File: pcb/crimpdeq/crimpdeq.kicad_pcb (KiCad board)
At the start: 4 copper layers, 30 x 30 mm, 55 parts, among them J10 A-_Cable_Pad, J11 E+_Cable_Pad, J12 E-_Cable_Pad, J2 USB4105-GF-A, J5 B-_Cable_Pad, J6 SW+_Cable_Pad, J7 B+_Cable_Pad, J8 SW-_Cable_Pad, J9 A+_Cable_Pad, Q2 DMG3415U, U1 ESP32-C3-MINI-1, U2 MCP73831T-2ACI/OT, U3 ADS1220, U5 MAX17048G+T10, U6 SY8088

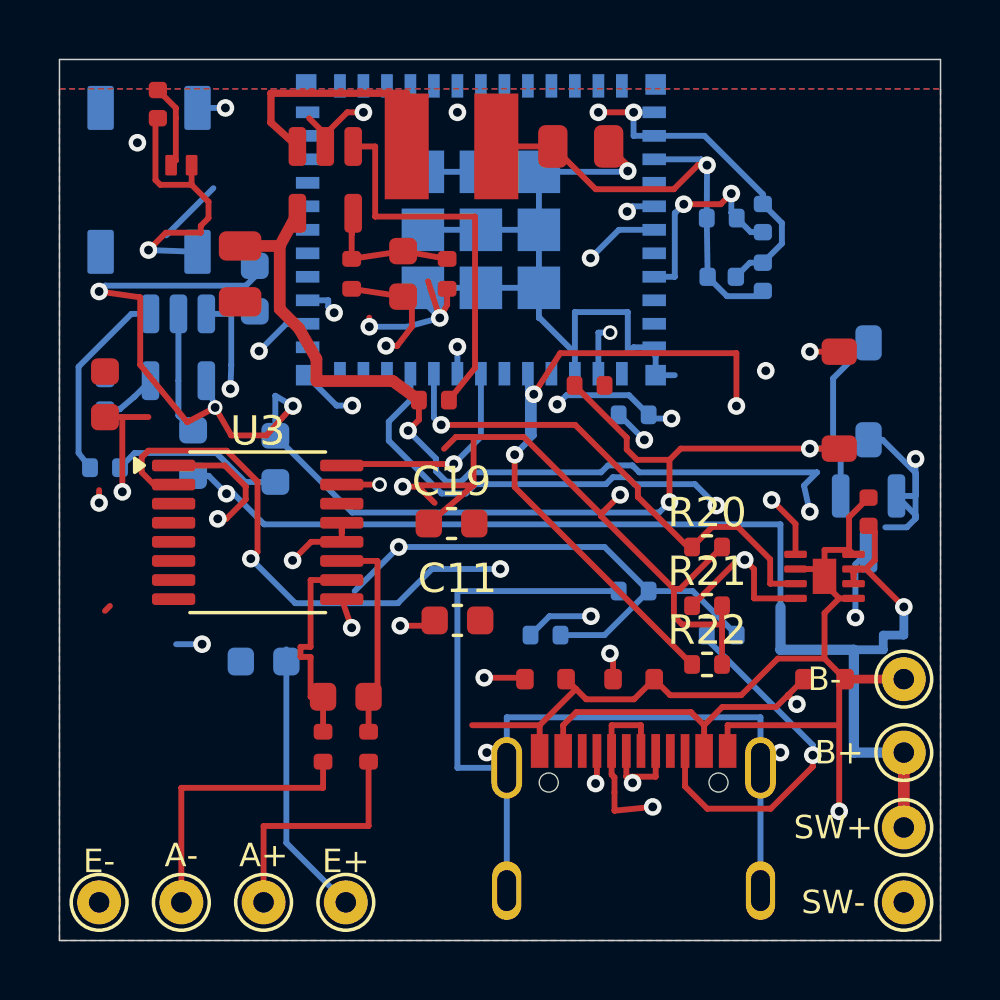
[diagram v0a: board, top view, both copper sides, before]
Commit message: fix: improve ADC bypassing and reconcile assembly metadata
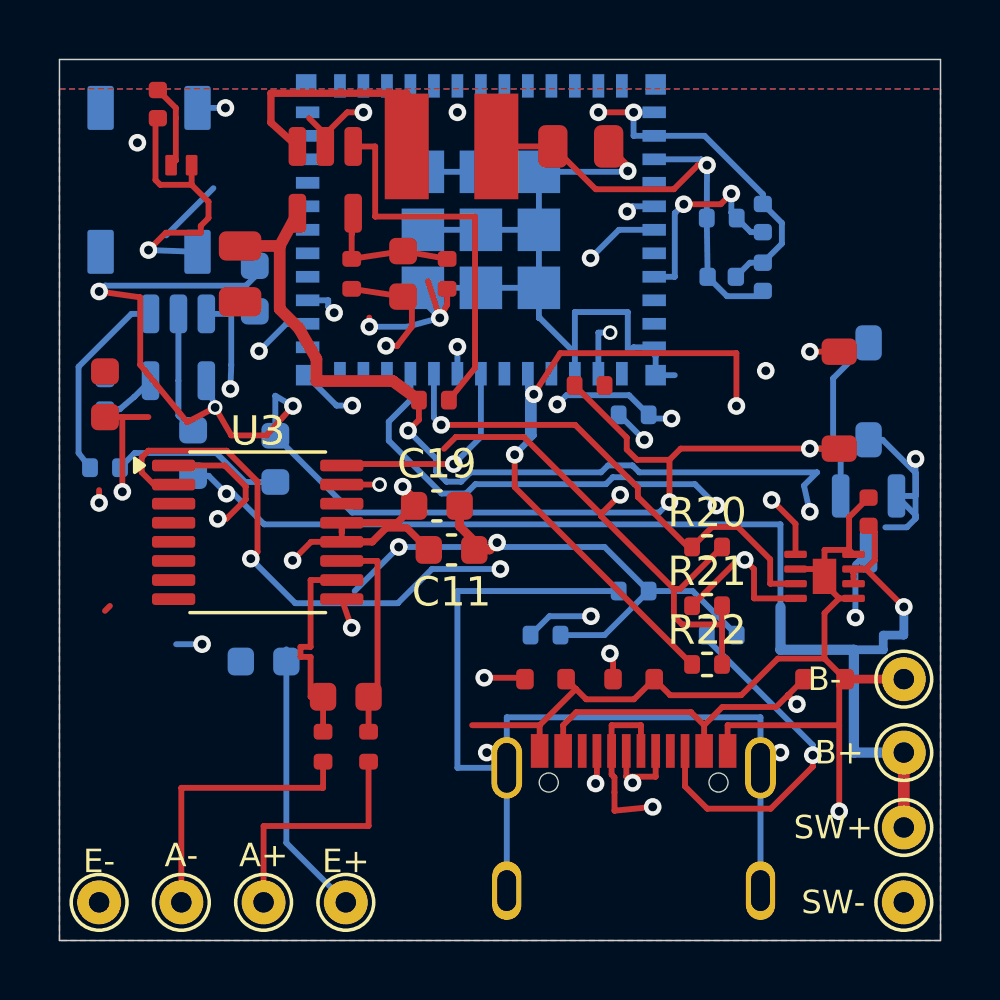
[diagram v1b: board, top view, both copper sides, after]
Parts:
- moved C11 2.41 mm to (140.8, 69.1)
- moved C19 0.78 mm to (140.3, 67.6)
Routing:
- net GND: track 134.6 -> 137.2 mm, vias 12 -> 13
- net IO5_SCK: track 26.4 -> 24.4 mm
- net +3V3: track 126.6 -> 124.8 mm, vias 10 -> 9
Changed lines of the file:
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@@
 			)
 		)
-		(property "LCSC" "C25741"
+		(property "LCSC" "C25076"
 			(at 0 0 270)
 			(unlocked yes)
@@
 	(footprint "C_0603_1608Metric"
 		(layer "F.Cu")
-		(at 141 71.5)
+		(at 140.8 69.1)
 		(descr "Capacitor SMD 0603 (1608 Metric), square (rectangular) end terminal, IPC-7351 nominal, (Body size source: IPC-SM-782 page 76, https://www.pcb-3d.com/wordpress/wp-content/uploads/ipc-sm-782a_amendment_1_and_2.pdf)")
 		(tags "capacitor")
 		(property "Reference" "C11"
-			(at 0 -1.43 0)
+			(at 0 1.43 0)
 			(layer "F.SilkS")
 			(effects
@@
 			)
 		)
-		(property "LCSC" "C25741"
+		(property "LCSC" "C25076"
 			(at 0 0 90)
 			(unlocked yes)
@@
 	(footprint "C_0603_1608Metric"
 		(layer "F.Cu")
-		(at 140.8 68.2)
+		(at 140.3 67.6)
 		(descr "Capacitor SMD 0603 (1608 Metric), square (rectangular) end terminal, IPC-7351 nominal, (Body size source: IPC-SM-782 page 76, https://www.pcb-3d.com/wordpress/wp-content/uploads/ipc-sm-782a_amendment_1_and_2.pdf)")
 		(tags "capacitor")
@@
 	)
 	(segment
+		(start 141.575 68.8)
+		(end 141.575 69.1)
+		(width 0.3)
+		(layer "F.Cu")
+		(net "GND")
+	)
+	(segment
 		(start 137.8 54.2)
 		(end 137.249 54.2)
@@
 	)
 	(segment
+		(start 141.075 68.3)
+		(end 141.575 68.8)
+		(width 0.3)
+		(layer "F.Cu")
+		(net "GND")
+	)
+	(segment
 		(start 154 73.7)
 		(end 154.2 73.5)
@@
 	)
 	(segment
+		(start 141.575 69.1)
+		(end 142.1 69.1)
+		(width 0.3)
+		(layer "F.Cu")
+		(net "GND")
+	)
+	(segment
 		(start 154.336 69.0983)
 		(end 154.488 69.25)
@@
 	)
 	(segment
+		(start 142.1 69.1)
+		(end 142.35 68.85)
+		(width 0.3)
+		(layer "F.Cu")
+		(net "GND")
+	)
+	(segment
+		(start 141.075 67.6)
+		(end 141.075 68.3)
+		(width 0.3)
+		(layer "F.Cu")
+		(net "GND")
+	)
+	(segment
 		(start 154 78)
 		(end 154 75.0683)
@@
 		(net "GND")
 	)
+	(via
+		(at 142.35 68.85)
+		(size 0.6)
+		(drill 0.3)
+		(layers "F.Cu" "B.Cu")
+		(net "GND")
+	)
 	(segment
 		(start 145 63.1)
@@
 	)
 	(segment
-		(start 141.55 65.256)
-		(end 141.55 66.9)
-		(width 0.2)
-		(layer "F.Cu")
-		(net "+3V3")
-	)
-	(segment
-		(start 141.55 66.9)
-		(end 139.671 66.9)
-		(width 0.2)
-		(layer "F.Cu")
-		(net "+3V3")
-	)
-	(segment
-		(start 140.025 68.2)
-		(end 141.55 66.9)
-		(width 0.2)
+		(start 139.525 67.3338)
+		(end 139.525 67.6)
+		(width 0.25)
 		(layer "F.Cu")
 		(net "+3V3")
 	)
 	(segment
-		(start 140.044 71.6807)
-		(end 139.054 71.6807)
-		(width 0.2)
+		(start 137.0625 68.825)
+		(end 138.1 68.825)
+		(width 0.25)
 		(layer "F.Cu")
 		(net "+3V3")
@@
 	)
 	(segment
-		(start 140.946 65.256)
-		(end 141.55 65.256)
+		(start 130.881 56.6686)
+		(end 131.95 56.6686)
 		(width 0.2)
 		(layer "F.Cu")
@@
 	)
 	(segment
-		(start 140.225 67.5)
-		(end 139.671 66.9458)
-		(width 0.2)
+		(start 138.575 68.35)
+		(end 139.275 68.35)
+		(width 0.25)
 		(layer "F.Cu")
 		(net "+3V3")
 	)
 	(segment
-		(start 130.881 56.6686)
-		(end 131.95 56.6686)
-		(width 0.2)
+		(start 138.1 68.825)
+		(end 138.575 68.35)
+		(width 0.25)
 		(layer "F.Cu")
 		(net "+3V3")
@@
 	)
 	(segment
-		(start 139.054 71.6807)
-		(end 139.054 71.6819)
-		(width 0.2)
+		(start 139.275 68.35)
+		(end 140.025 69.1)
+		(width 0.25)
 		(layer "F.Cu")
 		(net "+3V3")
@@
 	)
 	(segment
-		(start 139.671 66.9458)
-		(end 139.137 66.9458)
-		(width 0.2)
-		(layer "F.Cu")
-		(net "+3V3")
-	)
-	(segment
 		(start 150.01 71)
 		(end 150.01 71.6379)
@@
 	)
 	(segment
-		(start 139.671 66.9)
-		(end 139.671 66.9458)
-		(width 0.2)
-		(layer "F.Cu")
-		(net "+3V3")
-	)
-	(segment
 		(start 137.4 60.21)
 		(end 139.15 60.475)
@@
 	)
 	(segment
-		(start 129.591 67.1225)
-		(end 129.591 64.575)
-		(width 0.2)
+		(start 138.95 68.175)
+		(end 139.525 67.6)
+		(width 0.25)
 		(layer "F.Cu")
 		(net "+3V3")
 	)
 	(segment
-		(start 149.186 56)
-		(end 148.367 56.8187)
+		(start 129.591 67.1225)
+		(end 129.591 64.575)
 		(width 0.2)
 		(layer "F.Cu")
@@
 	)
 	(segment
-		(start 140.225 71.5)
-		(end 140.044 71.6807)
+		(start 149.186 56)
+		(end 148.367 56.8187)
 		(width 0.2)
 		(layer "F.Cu")
@@
 	)
 	(segment
-		(start 139.671 66.9458)
-		(end 139.671 66.946)
-		(width 0.2)
+		(start 139.137 66.9458)
+		(end 139.525 67.3338)
+		(width 0.25)
 		(layer "F.Cu")
 		(net "+3V3")
@@
 	)
 	(segment
+		(start 137.0625 68.175)
+		(end 138.95 68.175)
+		(width 0.25)
+		(layer "F.Cu")
+		(net "+3V3")
+	)
+	(segment
 		(start 136.02 68.825)
 		(end 136.541 68.825)
@@
 	)
 	(via
-		(at 139.054 71.6819)
-		(size 0.6)
-		(drill 0.3)
-		(layers "F.Cu" "B.Cu")
-		(net "+3V3")
-	)
-	(via
 		(at 137.4 71.75)
 		(size 0.6)
@@
 		(width 0.2)
 		(layer "In2.Cu")
-		(net "IO5_SCK")
-	)
-	(segment
-		(start 139.66 63.5214)
-		(end 138.216 64.9659)
-		(width 0.2)
-		(layer "In2.Cu")

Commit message: fix: keep digital routing outside ADC inputs
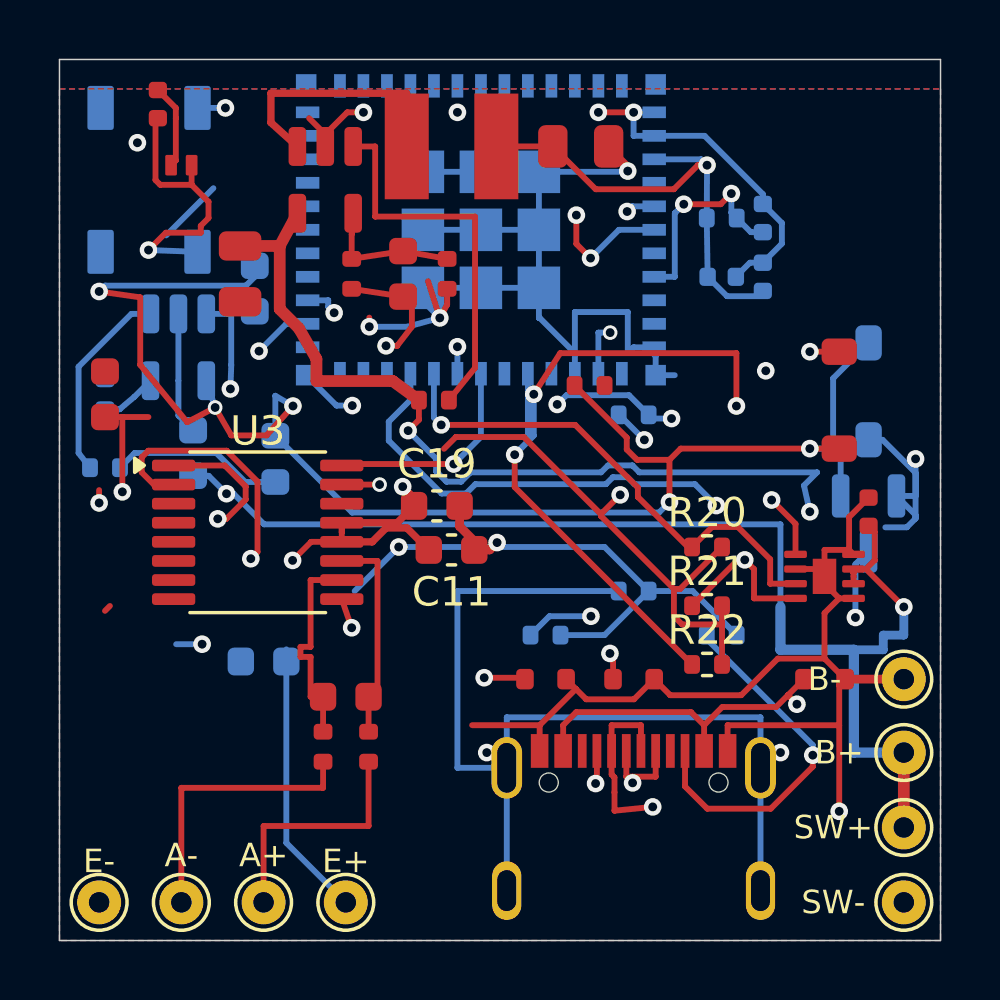
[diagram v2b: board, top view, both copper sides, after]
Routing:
- net IO3_CS: track 33.0 -> 37.6 mm
- net USB_D-: track 41.5 -> 40.2 mm
- net USB_D+: track 41.5 -> 40.9 mm
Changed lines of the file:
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@@
-	)
-	(segment
-		(start 136.802 70.4)
-		(end 136.802 61.026)
-		(width 0.2)
-		(layer "In2.Cu")
-		(net "USB_D+")
 	)
 	(segment
@@
 	)
 	(segment
-		(start 146.194 70.4)
-		(end 136.802 70.4)
+		(start 136.802 61.026)
+		(end 136.802 67.45)
+		(width 0.2)
+		(layer "In2.Cu")
+		(net "USB_D+")
+	)
+	(segment
+		(start 146.194 68.45)
+		(end 146.194 72.6247)
 		(width 0.2)
 		(layer "In2.Cu")
@@
 	)
 	(segment
+		(start 145.694 67.95)
+		(end 146.194 68.45)
+		(width 0.2)
+		(layer "In2.Cu")
+		(net "USB_D+")
+	)
+	(segment
 		(start 148.55 74.2)
 		(end 148.55 73.4)
@@
 	)
 	(segment
+		(start 137.302 67.95)
+		(end 145.694 67.95)
+		(width 0.2)
+		(layer "In2.Cu")
+		(net "USB_D+")
+	)
+	(segment
 		(start 146.965 77.0322)
 		(end 146.965 75)
@@
 	)
 	(segment
+		(start 136.802 67.45)
+		(end 137.302 67.95)
+		(width 0.2)
+		(layer "In2.Cu")
+		(net "USB_D+")
+	)
+	(segment
 		(start 150.5 75)
 		(end 150.5 74.2)
@@
 		(start 146.965 72.6247)
 		(end 146.194 72.6247)
-		(width 0.2)
-		(layer "In2.Cu")
-		(net "USB_D+")
-	)
-	(segment
-		(start 146.194 72.6247)
-		(end 146.194 70.4)
 		(width 0.2)
 		(layer "In2.Cu")
@@
 	)
 	(segment
-		(start 134.245 68)
-		(end 134.245 62.331)
+		(start 141.95 69.55)
+		(end 144.4 69.55)
 		(width 0.2)
 		(layer "In2.Cu")
@@
 	)
 	(segment
+		(start 134.245 62.331)
+		(end 134.245 67.85)
+		(width 0.2)
+		(layer "In2.Cu")
+		(net "USB_D-")
+	)
+	(segment
+		(start 134.245 67.85)
+		(end 134.745 68.35)
+		(width 0.2)
+		(layer "In2.Cu")
+		(net "USB_D-")
+	)
+	(segment
+		(start 134.745 68.35)
+		(end 140.75 68.35)
+		(width 0.2)
+		(layer "In2.Cu")
+		(net "USB_D-")
+	)
+	(segment
 		(start 144.9 77.85)
-		(end 144.9 70.85)
+		(end 144.9 73.4517)
 		(width 0.2)
 		(layer "In2.Cu")
@@
 	)
 	(segment
-		(start 136.1 68)
-		(end 134.245 68)
+		(start 140.75 68.35)
+		(end 141.95 69.55)
 		(width 0.2)
 		(layer "In2.Cu")
@@
 	)
 	(segment
+		(start 144.9 70.05)
+		(end 144.9 73.4517)
+		(width 0.2)
+		(layer "In2.Cu")
+		(net "USB_D-")
+	)
+	(segment
 		(start 144.9 73.4517)
 		(end 141.912 73.4517)
@@
 	)
 	(segment
-		(start 136.1 70.85)
-		(end 136.1 68)
-		(width 0.2)
-		(layer "In2.Cu")
-		(net "USB_D-")
-	)
-	(segment
-		(start 144.9 70.85)
-		(end 136.1 70.85)
+		(start 144.4 69.55)
+		(end 144.9 70.05)
 		(width 0.2)
 		(layer "In2.Cu")
@@
 	)
 	(segment
+		(start 145.05 58.6793)
+		(end 145.05 57.7)
+		(width 0.2)
+		(layer "F.Cu")
+		(net "IO3_CS")
+	)
+	(segment
 		(start 130.25 65.949)
 		(end 130.25 66.4586)
@@
 	)
 	(segment
+		(start 145.534 59.1633)
+		(end 145.05 58.6793)
+		(width 0.2)
+		(layer "F.Cu")
+		(net "IO3_CS")
+	)
+	(segment
 		(start 134.193 69.1705)
 		(end 134.193 66.772)
@@
 	)
 	(via
-		(at 142.462 69.75)
-		(size 0.6)
-		(drill 0.3)
-		(layers "F.Cu" "B.Cu")
-		(net "IO3_CS")
-	)
-	(segment
-		(start 135.48 70.9141)
-		(end 133.965 69.3987)
-		(width 0.2)
-		(layer "B.Cu")
+		(at 145.05 57.7)
+		(size 0.6)
+		(drill 0.3)
+		(layers "F.Cu" "B.Cu")
 		(net "IO3_CS")
 	)
@@
 	)
 	(segment
-		(start 138.971 70.9141)
-		(end 135.48 70.9141)
-		(width 0.2)
-		(layer "B.Cu")
-		(net "IO3_CS")
-	)
-	(segment
 		(start 147.7 58.2)
 		(end 146.498 58.2)
@@
 	)
 	(segment
-		(start 142.462 69.75)
-		(end 140.135 69.75)
-		(width 0.2)
-		(layer "B.Cu")
+		(start 144.85 57.9)
+		(end 141.55 57.9)
+		(width 0.2)
+		(layer "In2.Cu")
 		(net "IO3_CS")
 	)
 	(segment
-		(start 140.135 69.75)
-		(end 138.971 70.9141)
-		(width 0.2)
-		(layer "B.Cu")
+		(start 132.1 68.65)
+		(end 132.8487 69.3987)
+		(width 0.2)
+		(layer "In2.Cu")
 		(net "IO3_CS")
 	)
 	(segment
-		(start 145.534 66.678)
-		(end 142.462 69.75)
+		(start 141.55 57.9)
+		(end 139.9 59.55)
 		(width 0.2)
 		(layer "In2.Cu")
@@
 	)
 	(segment
-		(start 145.534 59.1633)
-		(end 145.534 66.678)
-		(width 0.2)
-		(layer "In2.Cu")
+		(start 145.05 57.7)
+		(end 144.85 57.9)
+		(width 0.2)
+		(layer "In2.Cu")
+		(net "IO3_CS")
+	)
+	(segment
+		(start 131.1 67)
+		(end 132.1 68)
+		(width 0.2)
+		(layer "In2.Cu")
+		(net "IO3_CS")
+	)
+	(segment
+		(start 131.1 62.9)
+		(end 131.1 67)
+		(width 0.2)
+		(layer "In2.Cu")
+		(net "IO3_CS")
+	)
+	(segment
+		(start 132.1 68)
+		(end 132.1 68.65)
+		(width 0.2)
+		(layer "In2.Cu")
+		(net "IO3_CS")
+	)
+	(segment
+		(start 134.45 59.55)
+		(end 131.1 62.9)
+		(width 0.2)
+		(layer "In2.Cu")
+		(net "IO3_CS")
+	)
+	(segment
+		(start 139.9 59.55)
+		(end 134.45 59.55)
+		(width 0.2)
+		(layer "In2.Cu")
+		(net "IO3_CS")
+	)
+	(segment
+		(start 132.8487 69.3987)
+		(end 133.965 69.3987)
+		(width 0.2)
+		(layer "In2.Cu")

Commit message: fix: remove USB pair routing overlap
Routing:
- net USB_D+: track 40.9 -> 37.7 mm
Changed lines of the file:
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@@
 	)
 	(segment
-		(start 148.55 73.4)
-		(end 146.965 73.4)
-		(width 0.2)
-		(layer "In2.Cu")
-		(net "USB_D+")
-	)
-	(segment
-		(start 146.965 73.4)
-		(end 148.548 73.4)
+		(start 148.548 72.8)
+		(end 148.548 74.2)
 		(width 0.2)
 		(layer "In2.Cu")
@@
 	)
 	(segment
-		(start 148.548 73.4)
-		(end 148.548 72.8)
-		(width 0.2)
-		(layer "In2.Cu")
-		(net "USB_D+")
-	)
-	(segment
 		(start 145.694 67.95)
 		(end 146.194 68.45)
 		(width 0.2)
 		(layer "In2.Cu")
-		(net "USB_D+")
-	)
-	(segment
-		(start 148.55 74.2)
-		(end 148.55 73.4)
-		(width 0.2)
-		(layer "In2.Cu")
